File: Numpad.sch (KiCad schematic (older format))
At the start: 56 parts, among them J1 USB_B_Mini, SW0 0, SW1 1, SW2 2, SW3 3, SW4 4, SW5 5, SW6 6, SW7 7, SW8 8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

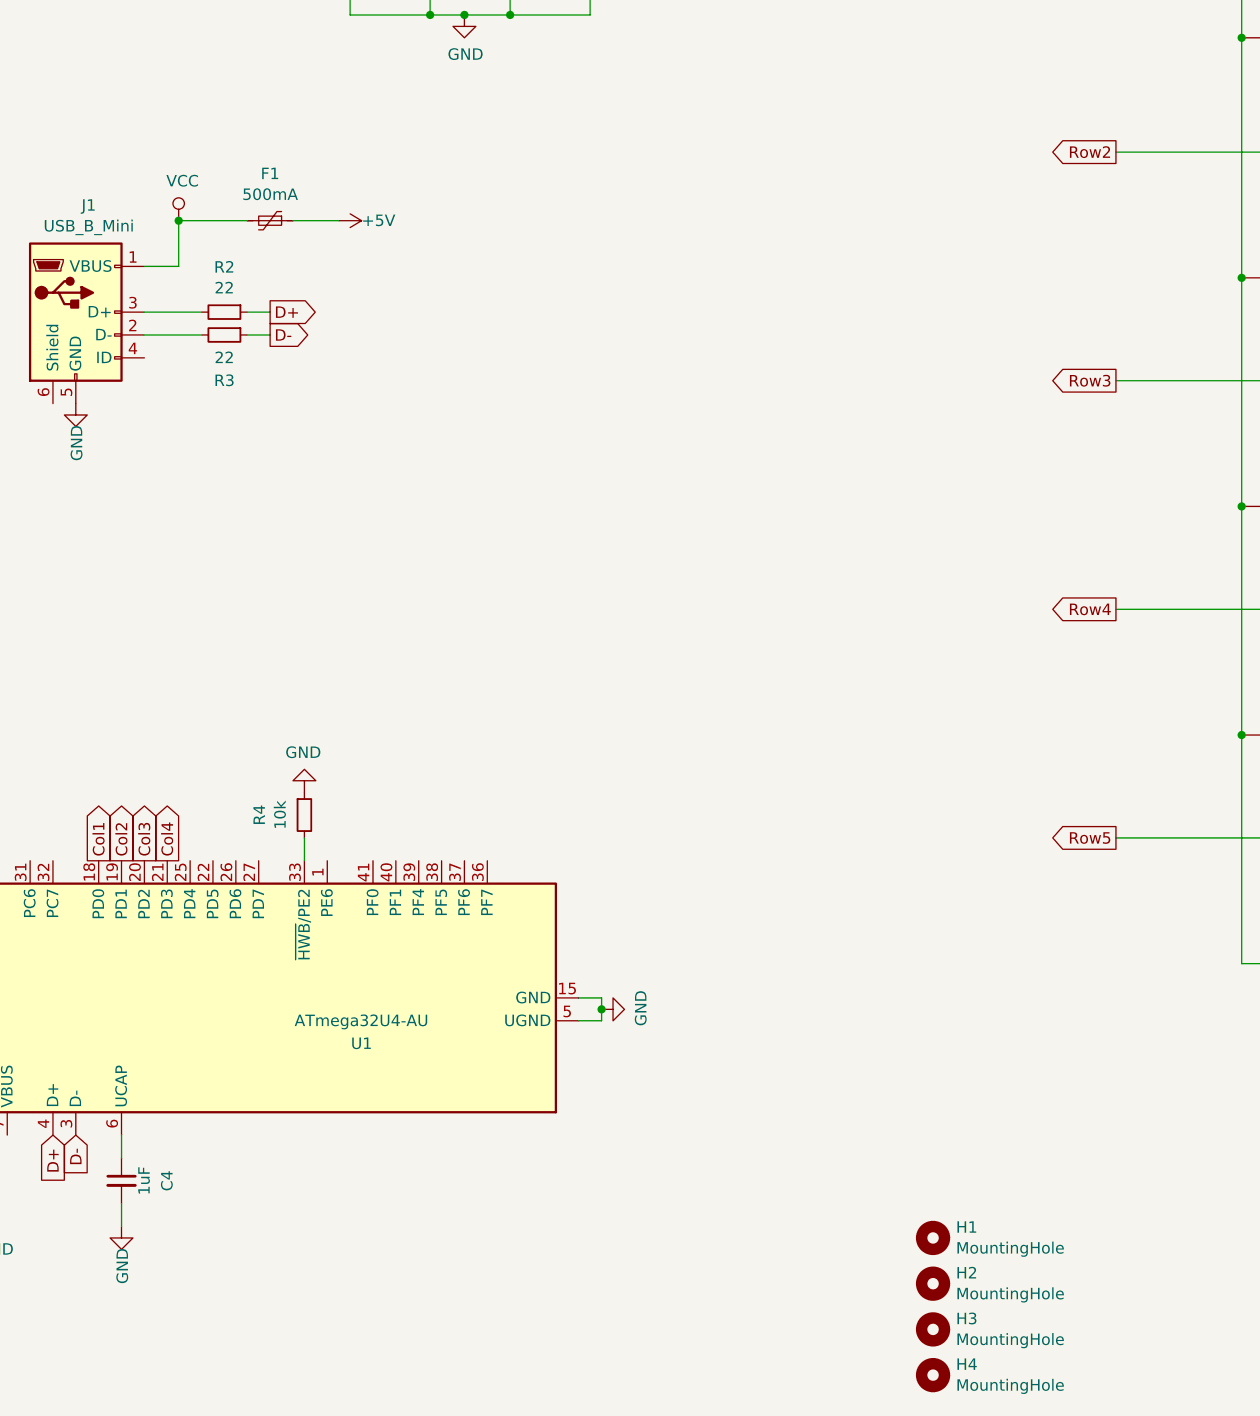
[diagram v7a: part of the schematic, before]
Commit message: moved some components around
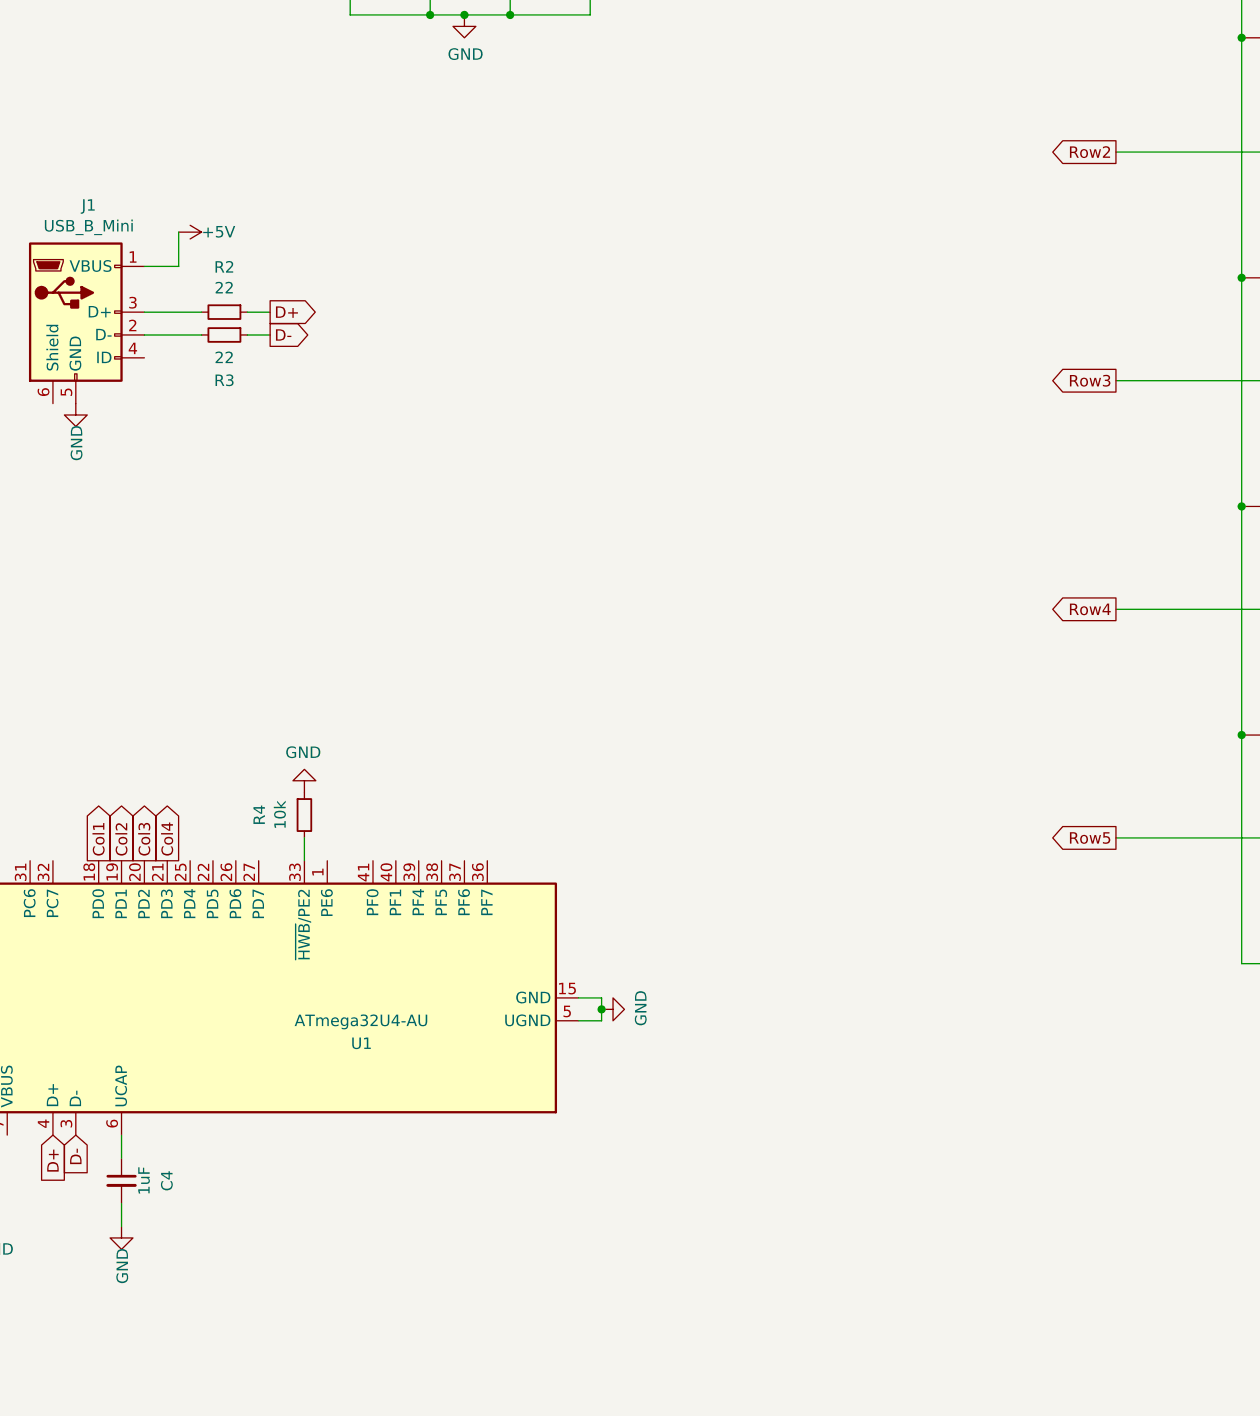
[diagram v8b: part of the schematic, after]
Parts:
- removed F1: 500mA, Fuse:Fuse_1206_3216Metric_Pad1.42x1.75mm_HandSolder, symbol Device:Polyfuse_Small
- removed H1, H2, H3, H4: MountingHole, MountingHole:MountingHole_3mm_Pad, symbol Mechanical:MountingHole
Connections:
- net VCC is gone; now on net +5V: J1.1 (VBUS)
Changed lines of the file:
@@
 L power:+5V #PWR04
 U 1 1 5D778839
-P 3550 2500
-F 0 "#PWR04" H 3550 2350 50  0001 C CNN
-F 1 "+5V" V 3550 2600 50  0000 L CNN
-F 2 "" H 3550 2500 50  0001 C CNN
-F 3 "" H 3550 2500 50  0001 C CNN
-	1    3550 2500
+P 2850 2550
+F 0 "#PWR04" H 2850 2400 50  0001 C CNN
+F 1 "+5V" V 2850 2650 50  0000 L CNN
+F 2 "" H 2850 2550 50  0001 C CNN
+F 3 "" H 2850 2550 50  0001 C CNN
+	1    2850 2550
 	0    1    1    0
 $EndComp
@@
 Text GLabel 2800 5300 1    50   Output ~ 0
 Col4
-$Comp
-L Mechanical:MountingHole H4
-U 1 1 5D799789
-P 6150 7550
-F 0 "H4" H 6250 7596 50  0000 L CNN
-F 1 "MountingHole" H 6250 7505 50  0000 L CNN
-F 2 "MountingHole:MountingHole_3mm_Pad" H 6150 7550 50  0001 C CNN
-F 3 "~" H 6150 7550 50  0001 C CNN
-	1    6150 7550
-	1    0    0    -1
-$EndComp
-$Comp
-L Mechanical:MountingHole H3
-U 1 1 5D79B1CB
-P 6150 7350
-F 0 "H3" H 6250 7396 50  0000 L CNN
-F 1 "MountingHole" H 6250 7305 50  0000 L CNN
-F 2 "MountingHole:MountingHole_3mm_Pad" H 6150 7350 50  0001 C CNN
-F 3 "~" H 6150 7350 50  0001 C CNN
-	1    6150 7350
-	1    0    0    -1
-$EndComp
-$Comp
-L Mechanical:MountingHole H2
-U 1 1 5D79EB2E
-P 6150 7150
-F 0 "H2" H 6250 7196 50  0000 L CNN
-F 1 "MountingHole" H 6250 7105 50  0000 L CNN
-F 2 "MountingHole:MountingHole_3mm_Pad" H 6150 7150 50  0001 C CNN
-F 3 "~" H 6150 7150 50  0001 C CNN
-	1    6150 7150
-	1    0    0    -1
-$EndComp
-$Comp
-L Mechanical:MountingHole H1
-U 1 1 5D79EDD6
-P 6150 6950
-F 0 "H1" H 6250 6996 50  0000 L CNN
-F 1 "MountingHole" H 6250 6905 50  0000 L CNN
-F 2 "MountingHole:MountingHole_3mm_Pad" H 6150 6950 50  0001 C CNN
-F 3 "~" H 6150 6950 50  0001 C CNN
-	1    6150 6950
-	1    0    0    -1
-$EndComp
 Text GLabel 2300 6500 3    50   Input ~ 0
 D+
@@
 	0    1    1    0
 $EndComp
-$Comp
-L Device:Polyfuse_Small F1
-U 1 1 5D84253D
-P 3250 2500
-F 0 "F1" V 3045 2500 50  0000 C CNN
-F 1 "500mA" V 3136 2500 50  0000 C CNN
-F 2 "Fuse:Fuse_1206_3216Metric_Pad1.42x1.75mm_HandSolder" H 3300 2300 50  0001 L CNN
-F 3 "~" H 3250 2500 50  0001 C CNN
-	1    3250 2500
-	0    1    1    0
-$EndComp
-$Comp
-L power:VCC #PWR0101
-U 1 1 5D846B17
-P 2850 2500
-F 0 "#PWR0101" H 2850 2350 50  0001 C CNN
-F 1 "VCC" H 2867 2673 50  0000 C CNN
-F 2 "" H 2850 2500 50  0001 C CNN
-F 3 "" H 2850 2500 50  0001 C CNN
-	1    2850 2500
-	1    0    0    -1
-$EndComp
 Wire Wire Line
 	2700 2700 2850 2700
 Wire Wire Line
-	2850 2700 2850 2500
-Wire Wire Line
-	2850 2500 3150 2500
-Connection ~ 2850 2500
-Wire Wire Line
-	3350 2500 3550 2500
+	2850 2700 2850 2550
 $EndSCHEMATC
